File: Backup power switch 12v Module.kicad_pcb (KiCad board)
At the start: 2 copper layers, 94.3 x 76.2 mm, 70 parts, among them J1 BAT/PWR IN, J2 External, J3 PWR OUT, J4 Barrel_Jack_MountingPin, J5 Esternal, J6 Barrel_Jack_MountingPin, J8 Barrel_Jack_MountingPin, K1 SRD-12VDC-SL-C, Q2 AO3401A, Q3 BSS138, U1 LM393, U2 INA219AxD, U3 INA219AxD, U4 LTV-817, U5 LTV-817, U6 CN3763, U7 ESP32-C3 Pro Mini, U8 AMS1117-3.3, U9 LMR14203

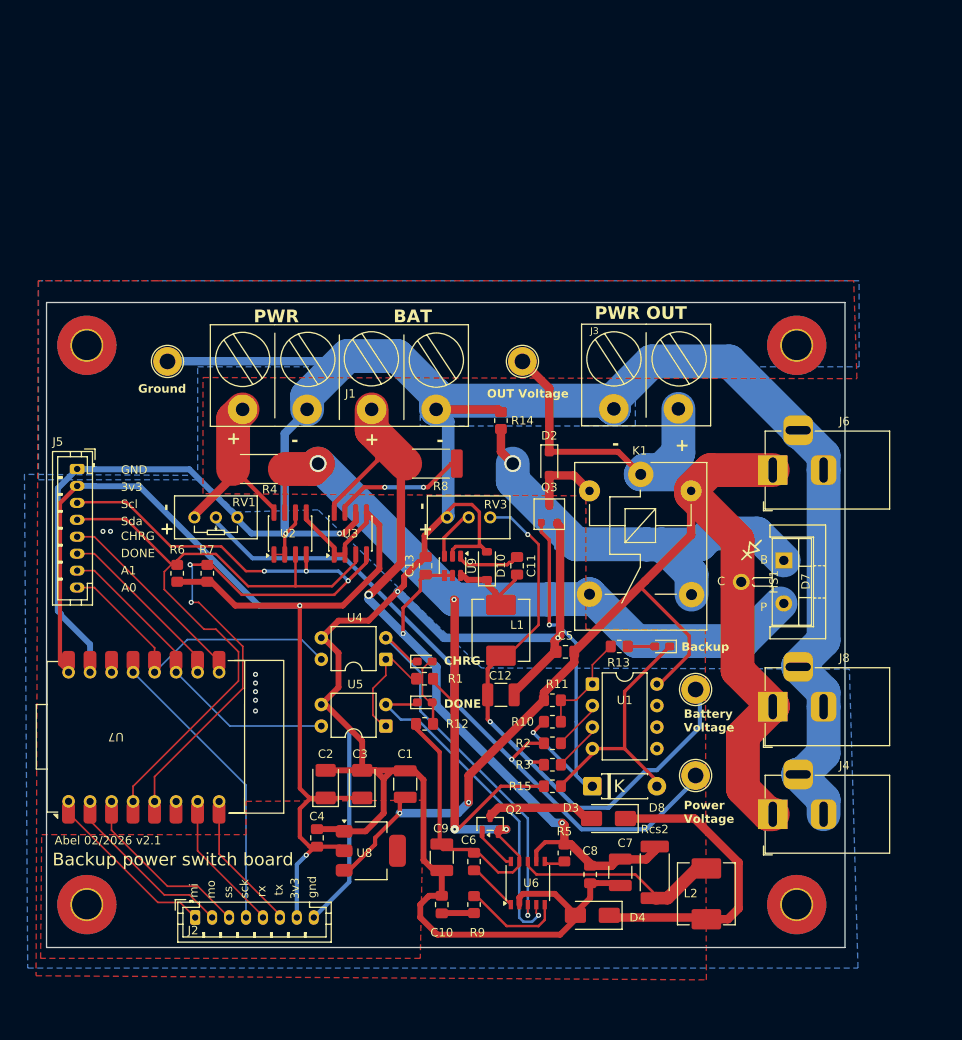
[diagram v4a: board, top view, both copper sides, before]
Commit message: Clean space for second relay
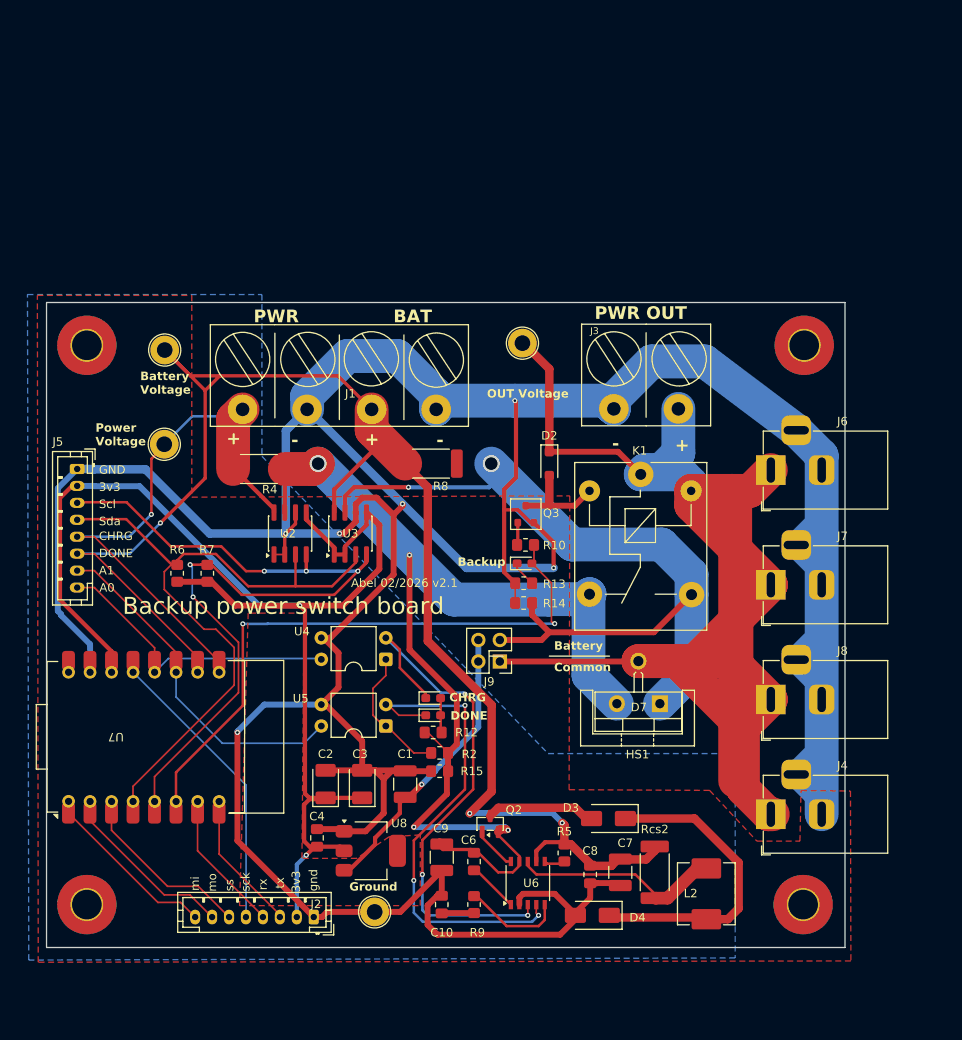
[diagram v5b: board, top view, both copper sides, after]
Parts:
- removed C11, C13: 2.2uF, Capacitor_SMD:C_0805_2012Metric_Pad1.18x1.45mm_HandSolder
- removed C12: 22uF, Capacitor_SMD:C_1210_3225Metric_Pad1.33x2.70mm_HandSolder
- removed C5: 100nF, Capacitor_SMD:C_0805_2012Metric_Pad1.18x1.45mm_HandSolder
- removed D10: 1N5819, Diode_SMD:D_SOD-123
- removed D8: 1N4744A, Diode_THT:D_DO-41_SOD81_P7.62mm_Horizontal
- removed L1: 47uH, Inductor_SMD:L_TechFuse_SL0650
- removed R1: 10K, Resistor_SMD:R_0805_2012Metric_Pad1.20x1.40mm_HandSolder
- removed R11: 10k, Resistor_SMD:R_0805_2012Metric_Pad1.20x1.40mm_HandSolder
- removed R3: 1k, Resistor_SMD:R_0805_2012Metric_Pad1.20x1.40mm_HandSolder
- removed RV1: 10k, PCM_Potentiometer_THT_AKL:Potentiometer_Bourns_3296W_Vertical
- removed RV3: 10k, Potentiometer_THT:Potentiometer_Bourns_3296W_Vertical
- removed U1: LM393, Package_DIP:DIP-8_W7.62mm
- removed U9: LMR14203, Package_TO_SOT_SMD:SOT-23-6
- added J7: Barrel_Jack_MountingPin, Connector_BarrelJack:BarrelJack_Horizontal, F.Cu at (174.7, 91.8)
- added J9: PWR SELECTOR, Connector_PinHeader_2.54mm:PinHeader_2x02_P2.54mm_Vertical, F.Cu at (142.7, 100.8)
- D6: value LED -> ON
- R13: value 1k -> 10k
- R2: value 1k -> 10K
- moved TP1 74.4 mm to (103.2, 64.1)
- moved TP2 73.9 mm to (103.1, 75.2)
- moved TP3 69.4 mm to (128.0, 130.4)
- moved HS1 29.3 mm to (159.0, 110.7), turned to 180 degrees
- moved D7 22.4 mm to (161.6, 105.8), turned to 180 degrees
- moved R14 21.7 mm to (145.6, 93.9), turned to 0 degrees
- moved R10 21.1 mm to (145.8, 87.1)
- moved D6 19.0 mm to (145.7, 89.3), turned to 0 degrees
- moved J2 14.0 mm to (120.8, 131.0), turned to 180 degrees
- moved R13 13.5 mm to (145.6, 91.6)
- moved R15 13.4 mm to (135.6, 113.8)
- moved R2 13.4 mm to (135.6, 111.6)
- moved D5 4.43 mm to (134.9, 105.2)
- moved Q3 2.78 mm to (145.8, 83.4)
- moved TP4 2.16 mm to (145.4, 63.2)
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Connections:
- net Net-(J5-Pin_3) renamed SCL
- net Net-(J5-Pin_4) renamed SDA
- net Net-(J5-Pin_7) renamed DONE_SIG
- net Net-(J5-Pin_8) renamed CHRG_SIG
- C1 pad 1: COMMON OUT 12 + -> Net-(J9-Pin_2)
- C6 pad 1: PWR OUT 12 + -> /PWR OUT 12 +
- C9 pad 1: PWR OUT 12 + -> /PWR OUT 12 +
- D6 pad 1: GNDPWR -> Net-(D6-K)
- D6 pad 2: Net-(D6-A) -> SIG
- D7 pad 3: PWR OUT 12 + -> /PWR OUT 12 +
- J2 pad 1: Net-(J2-Pin_1) -> GNDPWR
- J2 pad 2: Net-(J2-Pin_2) -> +3V3
- J2 pad 3: Net-(J2-Pin_3) -> TTL-TX
- J2 pad 4: Net-(J2-Pin_4) -> TTL-RX
- J2 pad 5: Net-(J2-Pin_5) -> SCK
- J2 pad 6: Net-(J2-Pin_6) -> SS
- J2 pad 7: +3V3 -> MOSI
- J2 pad 8: GNDPWR -> MISO
- J5 pad 5: Net-(J5-Pin_5) -> PWR IN 12 +
- J5 pad 6: Net-(J5-Pin_6) -> BAT IN 12 +
- K1 pad 3: PWR OUT 12 + -> /PWR OUT 12 +
- Q2 pad 2: PWR OUT 12 + -> /PWR OUT 12 +
- R12 pad 2: PWR OUT 12 + -> /PWR OUT 12 +
- R13 pad 1: SIG -> GNDPWR
- R13 pad 2: Net-(D6-A) -> Net-(D6-K)
- R14 pad 1: BAT OUT 12 + -> GNDPWR
- R14 pad 2: GNDPWR -> BAT OUT 12 +
- R15 pad 1: PWR OUT 12 + -> GNDPWR
- R15 pad 2: GNDPWR -> /PWR OUT 12 +
- R2 pad 1: Net-(U1A--) -> /PWR OUT 12 +
- R4 pad 2: PWR OUT 12 + -> /PWR OUT 12 +
- TP1 pad 1: /Battery voltage level limiter/BAT Low 12 + -> BAT IN 12 +
- TP2 pad 1: Net-(R2-Pad2) -> PWR IN 12 +
- U2 pad 7: PWR OUT 12 + -> /PWR OUT 12 +
- U4 pad 1: Net-(R1-Pad2) -> Net-(R2-Pad2)
- U5 pad 1: Net-(R1-Pad2) -> Net-(R2-Pad2)
- U6 pad 9: PWR OUT 12 + -> /PWR OUT 12 +
- U7 pad 0: Net-(J5-Pin_5) -> PWR IN 12 +
- U7 pad 1: Net-(J5-Pin_6) -> BAT IN 12 +
- U7 pad 10: unconnected-(U7-GPIO10-Pad10) -> SIG
- U7 pad 20: Net-(J2-Pin_5) -> TTL-RX
- U7 pad 21: Net-(J2-Pin_6) -> TTL-TX
- U7 pad 4: Net-(J2-Pin_4) -> SCK
- U7 pad 5: Net-(J2-Pin_1) -> MISO
- U7 pad 6: Net-(J2-Pin_2) -> MOSI
- U7 pad 7: Net-(J2-Pin_3) -> SS
- U7 pad P3: unconnected-(U7-VCC_3V-PadP3) -> +3V3
- U7 pad P5: +3V3 -> unconnected-(U7-VCC_5V-PadP5)
- U8 pad 3: COMMON OUT 12 + -> Net-(J9-Pin_2)
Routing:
- net PWR OUT 12 +: track 156.9 -> 0.00 mm, vias 4 -> 0
- net /PWR OUT 12 +: track 0.00 -> 131.7 mm, vias 0 -> 4
- net BAT IN 12 +: track 109.5 -> 190.6 mm
- net /Battery voltage level limiter/BAT Low 12 +: track 70.4 -> 0.00 mm, vias 3 -> 0
- net Net-(R2-Pad2): track 82.1 -> 16.1 mm, vias 1 -> 0
- net SIG: track 12.4 -> 73.0 mm, vias 0 -> 2
- net Net-(Q3-G): track 45.4 -> 2.67 mm, vias 2 -> 0
- net PWR IN 12 +: track 30.4 -> 71.1 mm, vias 0 -> 1
- net Net-(J9-Pin_2): track 0.00 -> 34.7 mm, vias 0 -> 1
- net SCK: track 0.00 -> 34.5 mm
- net Net-(J2-Pin_4): track 34.5 -> 0.00 mm
- net Net-(J5-Pin_5): track 26.1 -> 0.00 mm
- net BAT OUT 12 +: track 76.0 -> 101.6 mm, vias 3 -> 2
- net Net-(J5-Pin_6): track 23.2 -> 0.00 mm
- net Net-(J2-Pin_3): track 20.2 -> 0.00 mm
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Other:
- board text added: "Battery"
- board text added: "Common"
- board text removed: "B"
- board text removed: "C"
- board text removed: "P"

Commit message: Place second relay
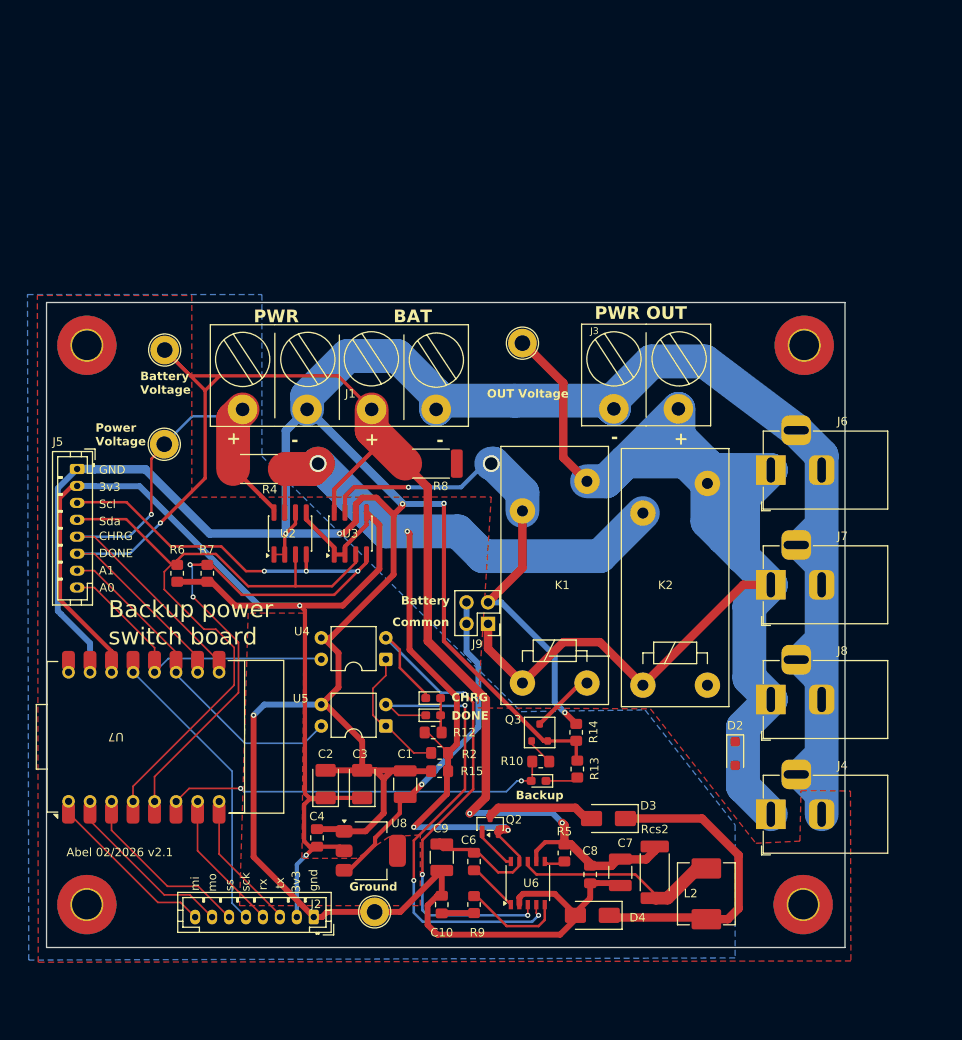
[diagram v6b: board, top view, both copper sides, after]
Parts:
- removed D7: MURF2060CT, PCM_Package_TO_SOT_THT_AKL_OneLayer:TO-220-3_Staggered_Vertical
- removed HS1: Heatsink, Heatsink:Heatsink_Stonecold_HS-S01_13.21x6.35mm
- added K2: SRD-12VDC-SL-C, Relay_THT:Relay_SPST_Schrack-RP-II-1-FormA_RM3.5mm, F.Cu at (159.6, 103.6)
- K1: footprint Relay_THT:Relay_SPDT_SANYOU_SRD_Series_Form_C -> Relay_THT:Relay_SPST_Schrack-RP-II-1-FormA_RM3.5mm
- moved D2 40.7 mm to (170.5, 111.7)
- moved K1 28.3 mm to (145.4, 103.4), turned to 90 degrees
- moved Q3 25.8 mm to (147.4, 109.2)
- moved D6 25.7 mm to (147.3, 114.9), turned to 180 degrees
- moved R10 25.6 mm to (147.6, 112.6), turned to 0 degrees
- moved R13 22.8 mm to (151.9, 113.5), turned to -90 degrees
- moved R14 16.5 mm to (151.8, 109.2), turned to 90 degrees
- moved J9 4.66 mm to (141.4, 96.4)
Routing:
- net BAT OUT 12 +: track 101.6 -> 64.4 mm, vias 2 -> 3
- net SIG: track 73.0 -> 45.6 mm
- net COMMON OUT 12 +: track 195.3 -> 180.1 mm
- net GNDPWR: track 507.5 -> 493.5 mm, vias 6 -> 5
- net /PWR OUT 12 +: track 131.7 -> 126.3 mm
- net Net-(J9-Pin_2): track 34.7 -> 39.4 mm
- net Net-(D2-A): track 11.9 -> 7.59 mm
- net DONE_SIG: track 41.2 -> 39.6 mm
- net Net-(D6-K): track 3.07 -> 3.86 mm
- net Net-(Q3-G): track 2.67 -> 3.29 mm
- net BAT IN 12 +: track 190.6 -> 190.1 mm
- net Net-(D3-K): track 36.9 -> 37.4 mm

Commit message: Connect srcond relay
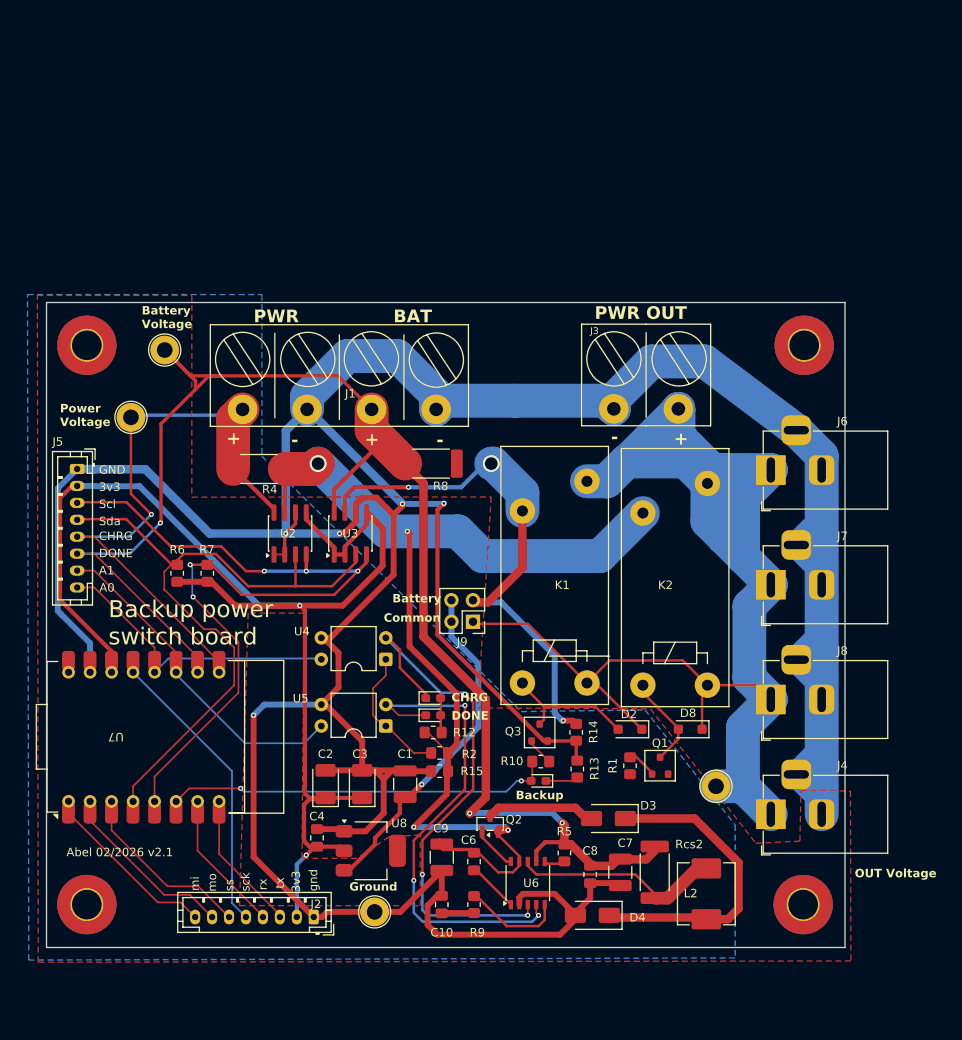
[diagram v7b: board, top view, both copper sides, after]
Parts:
- added D8: 1N4007W (A7), Diode_SMD:D_SOD-123F, F.Cu at (165.2, 108.8)
- added Q1: BSS138, PCM_Package_TO_SOT_SMD_AKL:SOT-23, F.Cu at (161.7, 113.1)
- added R1: 1k, Resistor_SMD:R_0805_2012Metric_Pad1.20x1.40mm_HandSolder, F.Cu at (158.1, 113.1)
- J5: value Esternal -> External
- K1, K2: value SRD-12VDC-SL-C -> SMIH-S-112LM
- R13: value 10k -> 1k
- moved TP4 57.1 mm to (168.3, 115.6)
- moved D2 12.7 mm to (158.1, 108.8), turned to 180 degrees
- moved TP2 5.06 mm to (99.2, 72.0)
- moved J9 1.80 mm to (139.6, 96.1)
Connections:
- K1 pad A1: COMMON OUT 12 + -> Net-(D2-A)
- K1 pad A2: Net-(D2-A) -> COMMON OUT 12 +
- K2 pad A1: COMMON OUT 12 + -> Net-(D8-A)
- K2 pad A2: unconnected-(K2-PadA2) -> COMMON OUT 12 +
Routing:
- net Net-(D8-A): track 0.00 -> 11.1 mm
- net Net-(D2-A): track 7.59 -> 16.0 mm
- net COMMON OUT 12 +: track 180.1 -> 172.2 mm
- net PWR IN 12 +: track 71.1 -> 77.3 mm
- net BAT OUT 12 +: track 64.4 -> 68.9 mm
- net Net-(Q1-G): track 0.00 -> 3.75 mm
- net Net-(J9-Pin_2): track 39.4 -> 40.4 mm
- net GNDPWR: track 493.5 -> 494.1 mm
- net Net-(D3-K): track 37.4 -> 36.9 mm
